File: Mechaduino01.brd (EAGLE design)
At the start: 41.9 x 41.9 mm, 64 parts, among them IC1 SAMD21G18A-AUT, Q1 BSS138, Q2 NFET, Q3 BSS138, Q4 BSS138, Q5 BSS138, U1 TLV70233PDBVR, Y1 32,768Khz

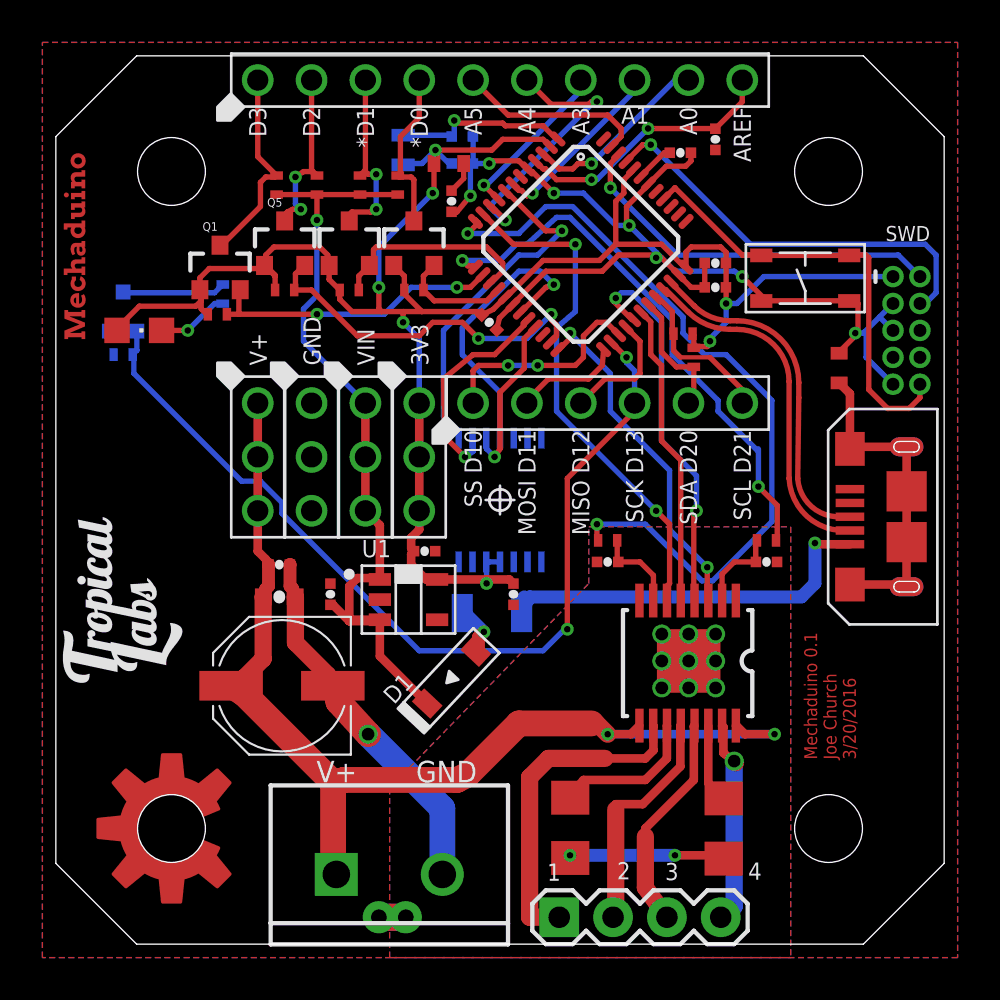
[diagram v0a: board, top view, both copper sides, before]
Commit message: passes DRC
should still double check
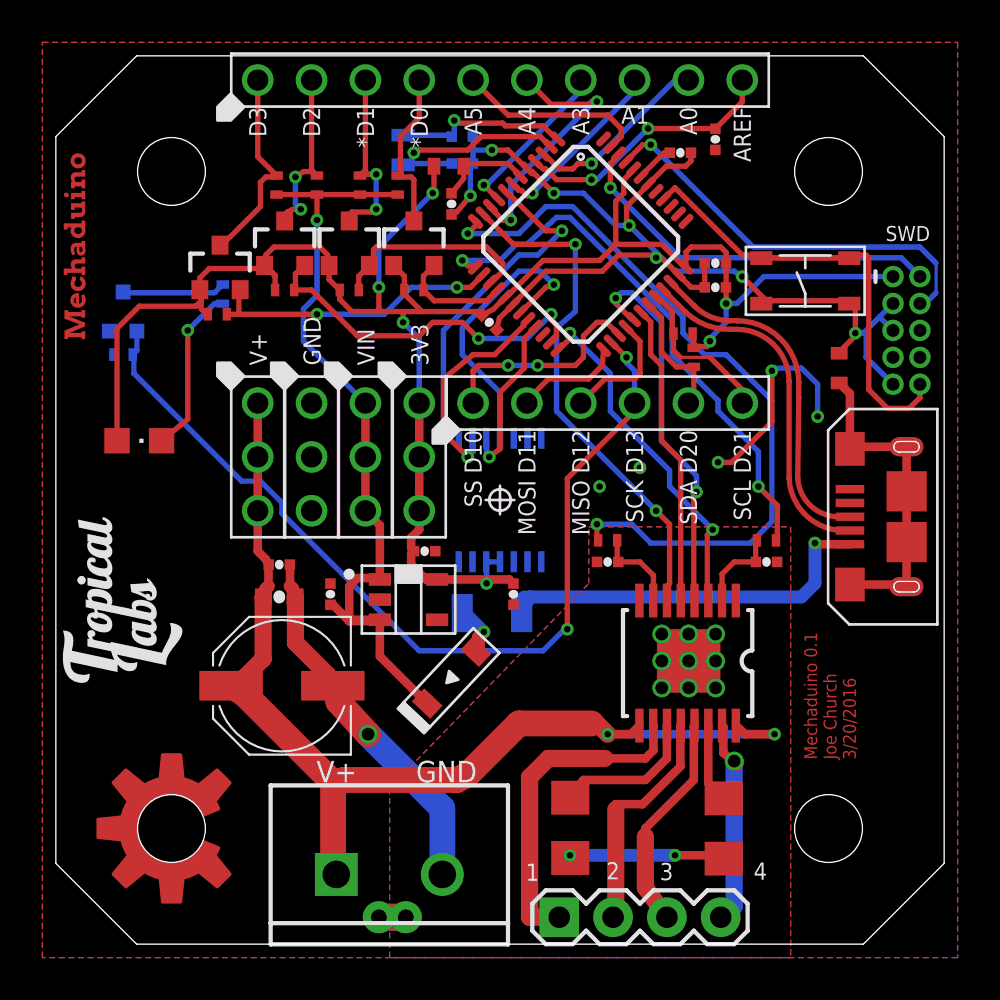
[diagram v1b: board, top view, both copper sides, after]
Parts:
- moved LED1 5.21 mm to (3.94, 23.7)
- moved C5 0.13 mm to (18.7, 34.9)
- moved SW2 0.13 mm to (35.4, 31.3)
- moved L2 0.13 mm to (18.5, 36.7)
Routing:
- net GND: track 53.4 -> 63.8 mm, vias 7 -> 12
- net 3.3V: track 88.4 -> 93.4 mm
- net N$1: track 3.42 -> 7.97 mm
- net VDDANA: track 1.52 -> 4.51 mm
- net ARDUINO_D9----VREF1: track 37.1 -> 35.7 mm
- net PA01_XOUT32: track 8.62 -> 9.77 mm

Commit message: minor fixes
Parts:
- moved U$5 2.69 mm to (1.91, 25.8)
- moved U$3 2.43 mm to (7.75, 14.0)
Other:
- board text added: "Mechaduino 0.2 Joe Church 2/2/2017"
- board text removed: "Mechaduino 0.1 Joe Church 3/20/2016"
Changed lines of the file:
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@@
 <text x="28.808678125" y="3.42391875" size="0.8128" layer="21" align="center">3</text>
 <text x="26.286459375" y="3.462021875" size="0.8128" layer="21" rot="R180" align="center">2</text>
-<text x="37.746940625" y="8.7122" size="0.6096" layer="1" font="vector" ratio="13" rot="R90">Mechaduino 0.1
+<text x="37.746940625" y="8.9662" size="0.6096" layer="1" font="vector" ratio="13" rot="R90">Mechaduino 0.2
 Joe Church
-3/20/2016</text>
+2/2/2017</text>
 <text x="12.2936" y="7.6327" size="1.016" layer="21">V+</text>
 <text x="22.481540625" y="3.395978125" size="0.8128" layer="21" align="center">1</text>
-<text x="37.746940625" y="8.7122" size="0.6096" layer="29" font="vector" ratio="13" rot="R90">Mechaduino 0.1
+<text x="37.746940625" y="8.9662" size="0.6096" layer="29" font="vector" ratio="13" rot="R90">Mechaduino 0.2
 Joe Church
-3/20/2016</text>
+2/2/2017</text>
 <rectangle x1="26.543" y1="10.541" x2="33.147" y2="16.002" layer="30"/>
 <text x="36.83" y="-9.525" size="1.27" layer="49" font="vector" align="center">Joe Church</text>
@@
 <attribute name="NAME" x="15.494" y="2.159" size="0.762" layer="51" ratio="10" rot="R270"/>
 </element>
-<element name="U$3" library="stepper_servo_prototype_1" package="LOGO3" value="TROPICAL_LABS_LOGO_1LOGO3" x="6.096" y="12.192" rot="R90"/>
+<element name="U$3" library="stepper_servo_prototype_1" package="LOGO3" value="TROPICAL_LABS_LOGO_1LOGO3" x="7.747" y="13.97" rot="R90"/>
 <element name="J1" library="MF_Connectors" package="MICROUSB-RIGHT" value="" x="38.735" y="20.166" locked="yes" smashed="yes" rot="R90"/>
 <element name="R16" library="adafruit" package="R0402-VISHAY" value="100K" x="3.175" y="27.813" rot="MR180"/>
@@
 <attribute name="NAME" x="9.144" y="27.305" size="0.8128" layer="25" font="vector" ratio="16" rot="R270" align="bottom-right"/>
 </element>
-<element name="U$5" library="stepper_servo_prototype_1" package="MECHADUINO_LOGO" value="MECHADUINO_LOGO" x="1.524" y="28.448" rot="R90"/>
+<element name="U$5" library="stepper_servo_prototype_1" package="MECHADUINO_LOGO" value="MECHADUINO_LOGO" x="1.905" y="25.781" rot="R90"/>
 <element name="SW2" library="MF_Switches" package="TACT4.2MM" value="" x="35.3568" y="31.2928" smashed="yes"/>
 <element name="Q5" library="SparkFun" package="SOT23-3" value="BSS138" x="10.795" y="33.02" smashed="yes"/>

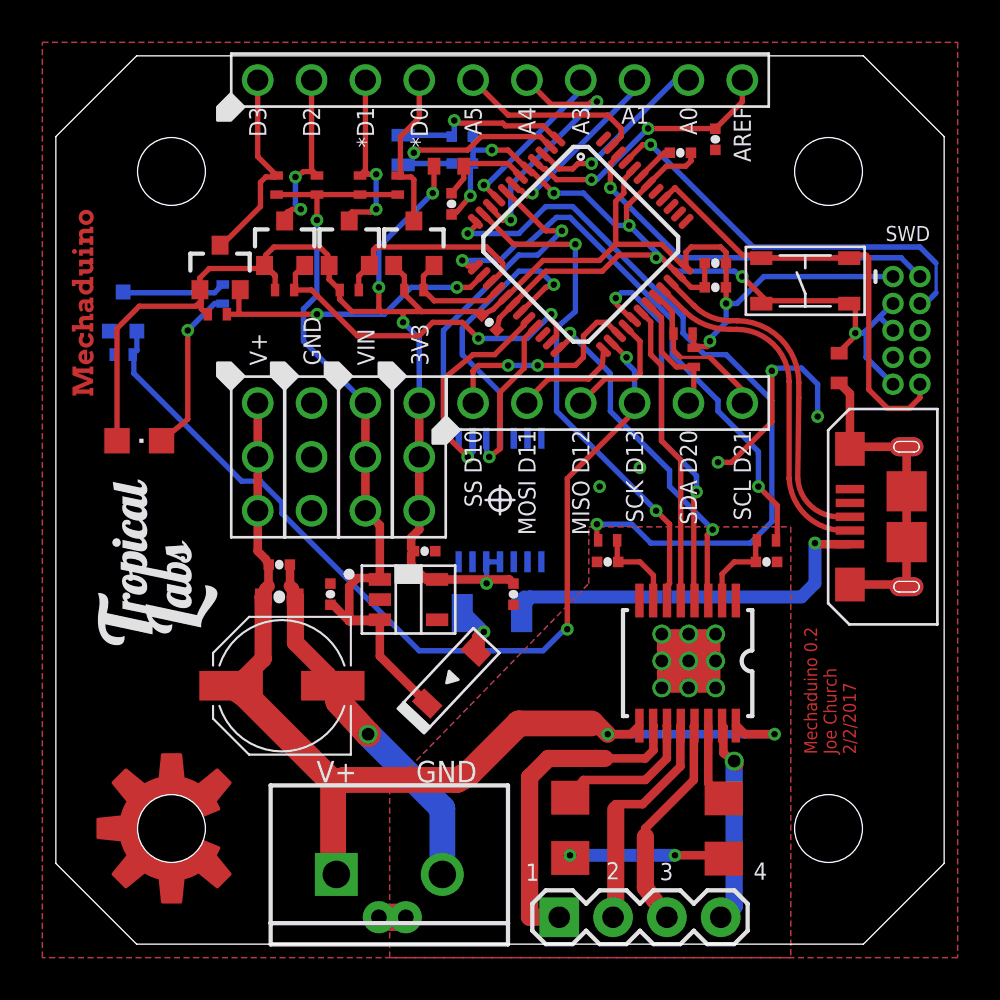
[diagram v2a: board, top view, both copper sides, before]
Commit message: moved button
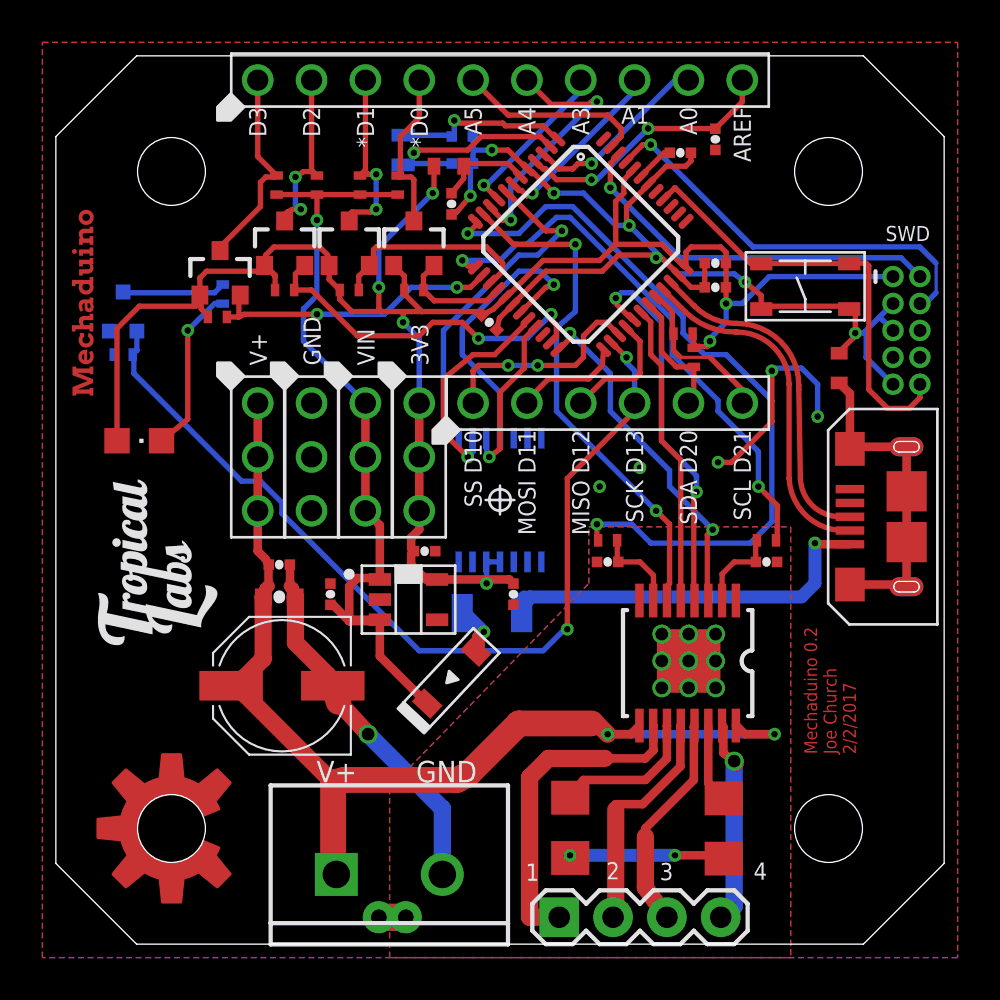
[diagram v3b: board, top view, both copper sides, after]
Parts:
- moved SW2 0.25 mm to (35.4, 31.0)
- moved Q1 0.25 mm to (7.75, 31.6)
- moved R1 0.13 mm to (7.62, 29.6)
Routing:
- net 3.3V: track 93.4 -> 94.0 mm

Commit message: updated caps
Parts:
- C7, C8: value 22pF -> 18pF
- moved R7 0.13 mm to (29.6, 28.7)
- moved R8 0.13 mm to (30.1, 27.6)
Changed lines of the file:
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@@
 <element name="C2" library="swift" package="0402-CAP" value="0.1uF" x="31.115" y="30.988" smashed="yes" rot="R180"/>
 <element name="C5" library="swift" package="0402-CAP" value="0.1uF" x="18.669" y="34.925" smashed="yes" rot="R270"/>
-<element name="C7" library="swift" package="0402-CAP" value="22pF" x="19.177" y="38.1" smashed="yes" rot="MR0"/>
-<element name="C8" library="swift" package="0402-CAP" value="22pF" x="19.177" y="36.83" smashed="yes" rot="MR0"/>
+<element name="C7" library="swift" package="0402-CAP" value="18pF" x="19.177" y="38.1" smashed="yes" rot="MR0"/>
+<element name="C8" library="swift" package="0402-CAP" value="18pF" x="19.177" y="36.83" smashed="yes" rot="MR0"/>
 <element name="LED1" library="Opto" package="CHIPLED_0805" value="Green" x="3.937" y="23.749" smashed="yes" rot="R270">
 <attribute name="CASE" value="" x="3.937" y="23.749" size="1.778" layer="27" rot="R270" display="off"/>
@@
 <attribute name="PART_NUMBER" value="KPT-2012YC" x="3.937" y="23.749" size="1.778" layer="27" rot="R270" display="off"/>
 </element>
-<element name="R7" library="adafruit" package="R0402-VISHAY" value="4.7K" x="29.591" y="28.8036" smashed="yes"/>
-<element name="R8" library="adafruit" package="R0402-VISHAY" value="4.7K" x="30.099" y="27.686" smashed="yes" rot="R90"/>
+<element name="R7" library="adafruit" package="R0402-VISHAY" value="4.7K" x="29.591" y="28.6766" smashed="yes"/>
+<element name="R8" library="adafruit" package="R0402-VISHAY" value="4.7K" x="30.099" y="27.559" smashed="yes" rot="R90"/>
 <element name="C1" library="swift" package="0402-CAP" value="0.1uF" x="31.115" y="32.131" smashed="yes" rot="R180"/>
 <element name="C3" library="swift" package="0402-CAP" value="0.1uF" x="20.447" y="29.337" smashed="yes" rot="R135"/>
@@
 <contactref element="R1" pad="2"/>
 <wire x1="30.099" y1="28.194" x2="30.099" y2="28.7456" width="0.254" layer="1"/>
-<wire x1="30.099" y1="28.7456" x2="30.041" y2="28.8036" width="0.254" layer="1"/>
-<wire x1="30.861" y1="28.448" x2="30.734" y2="28.575" width="0.254" layer="16"/>
-<wire x1="30.861" y1="28.321" x2="30.861" y2="28.448" width="0.254" layer="1"/>
-<wire x1="30.734" y1="28.194" x2="30.861" y2="28.321" width="0.254" layer="1"/>
+<wire x1="30.099" y1="28.7456" x2="30.041" y2="28.6766" width="0.254" layer="1"/>
+<wire x1="30.734" y1="28.194" x2="30.861" y2="28.448" width="0.254" layer="1"/>
 <wire x1="30.099" y1="28.194" x2="30.734" y2="28.194" width="0.254" layer="1"/>
-<wire x1="30.099" y1="28.194" x2="30.099" y2="28.136" width="0.254" layer="1"/>
+<wire x1="30.099" y1="28.194" x2="30.099" y2="28.009" width="0.254" layer="1"/>
 <via x="30.861" y="28.448" extent="1-16" drill="0.3048" diameter="0.254"/>
 <wire x1="31.623" y1="29.337" x2="31.623" y2="30.226" width="0.254" layer="16"/>
@@
 <wire x1="29.464" y1="16.2291" x2="29.4827" y2="16.2104" width="0.254" layer="1"/>
 <wire x1="27.611103125" y1="29.820340625" x2="28.067" y2="29.36444375" width="0.254" layer="1"/>
-<wire x1="28.067" y1="29.36444375" x2="28.067" y2="27.813" width="0.254" layer="1"/>
-<wire x1="28.067" y1="27.813" x2="28.575" y2="27.305" width="0.254" layer="1"/>
-<wire x1="28.575" y1="27.305" x2="28.575" y2="23.749" width="0.254" layer="1"/>
+<wire x1="28.067" y1="29.36444375" x2="28.067" y2="27.559" width="0.254" layer="1"/>
+<wire x1="28.067" y1="27.559" x2="28.575" y2="27.051" width="0.254" layer="1"/>
+<wire x1="28.575" y1="27.051" x2="28.575" y2="23.749" width="0.254" layer="1"/>
 <wire x1="28.575" y1="23.749" x2="29.4827" y2="22.8413" width="0.254" layer="1"/>
 <wire x1="29.4827" y1="22.8413" x2="29.4827" y2="16.2104" width="0.254" layer="1"/>
@@
 <contactref element="R8" pad="1"/>
 <contactref element="J3" pad="P$5"/>
-<wire x1="30.099" y1="27.236" x2="29.279" y2="27.236" width="0.254" layer="1"/>
-<wire x1="29.279" y1="27.236" x2="28.575" y2="27.94" width="0.254" layer="1"/>
-<wire x1="28.575" y1="27.94" x2="28.575" y2="29.56355" width="0.254" layer="1"/>
+<wire x1="30.099" y1="27.109" x2="29.279" y2="27.109" width="0.254" layer="1"/>
+<wire x1="29.279" y1="27.109" x2="28.575" y2="27.813" width="0.254" layer="1"/>
+<wire x1="28.575" y1="27.813" x2="28.575" y2="29.56355" width="0.254" layer="1"/>
 <wire x1="28.575" y1="29.56355" x2="27.96465625" y2="30.17389375" width="0.254" layer="1"/>
 <wire x1="29.845" y1="25.527" x2="30.099" y2="25.781" width="0.254" layer="1"/>
-<wire x1="30.099" y1="25.781" x2="30.099" y2="27.236" width="0.254" layer="1"/>
+<wire x1="30.099" y1="25.781" x2="30.099" y2="27.109" width="0.254" layer="1"/>
 </signal>
 <signal name="ARDUINO_D21_SCL">
@@
 <contactref element="R7" pad="1"/>
 <contactref element="J3" pad="P$6"/>
-<wire x1="29.083" y1="28.829" x2="29.141" y2="28.8036" width="0.254" layer="1"/>
+<wire x1="29.083" y1="28.829" x2="29.141" y2="28.6766" width="0.254" layer="1"/>
 <wire x1="29.083" y1="29.845" x2="29.083" y2="28.829" width="0.254" layer="1"/>
 <wire x1="28.321" y1="30.607" x2="29.083" y2="29.845" width="0.254" layer="1"/>
 <wire x1="28.321" y1="30.607" x2="28.318209375" y2="30.527446875" width="0.254" layer="1"/>
-<wire x1="29.141" y1="28.8036" x2="29.141" y2="28.009" width="0.254" layer="1"/>
-<wire x1="29.141" y1="28.009" x2="29.464" y2="27.686" width="0.254" layer="1"/>
+<wire x1="29.141" y1="28.6766" x2="29.141" y2="28.009" width="0.254" layer="1"/>
+<wire x1="29.141" y1="28.009" x2="29.591" y2="27.559" width="0.254" layer="1"/>
 <wire x1="32.385" y1="25.527" x2="32.385" y2="26.162" width="0.254" layer="1"/>
-<wire x1="32.385" y1="26.162" x2="30.861" y2="27.686" width="0.254" layer="1"/>
-<wire x1="29.464" y1="27.686" x2="30.861" y2="27.686" width="0.1524" layer="1"/>
+<wire x1="32.385" y1="26.162" x2="30.988" y2="27.559" width="0.254" layer="1"/>
+<wire x1="29.591" y1="27.559" x2="30.988" y2="27.559" width="0.1524" layer="1"/>
 </signal>
 <signal name="HEADER_MOSI">

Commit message: reday to order
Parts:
- LOGO4: value OSHW-LOGOL-COPPER -> OSHW-LOGOMOD; device SparkFun-Aesthetics:OSHW-LOGO-L_COPPER -> SparkFun-Aesthetics:OSHW_LOGO_COPPER_MOD
- moved C19 0.64 mm to (16.8, 18.5), turned to 180 degrees
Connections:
- new net A: U$4.6
- new net B: U$4.7
- new net I: U$4.14
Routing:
- net A: track 0.00 -> 2.39 mm, vias 0 -> 1
- net N$16: track 12.7 -> 10.4 mm
- net N$2: track 3.73 -> 5.91 mm, vias 0 -> 1
- net I: track 0.00 -> 1.62 mm, vias 0 -> 1
- net ARDUINO_D2: track 17.1 -> 18.1 mm
- net B: track 0.00 -> 0.84 mm, vias 0 -> 1
- net 3.3V: track 93.9 -> 93.4 mm
- net N$4: vias 0 -> 1
